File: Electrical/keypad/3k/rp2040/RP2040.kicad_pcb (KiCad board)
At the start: 4 copper layers, 64.2 x 66.2 mm, 95 parts, among them J1 Conn_01x04_Socket, J2 Conn_01x04_Socket, P1 USB-TYPE-C-016, Q1 BSS138, Q2 BSS138, SW1 KAN0644-0551B1-A, SW2 KAN0644-0551B1-A, SW3 KAN0644-0551B1-A, SW4 TS-1187A-B-A-B, SW5 TS-1187A-B-A-B, U1 ME6212C33M5G, U2 W25Q16JVSS, U3 PRTR5V0U2X, U4 RP2040, U5 SLSS49E, U6 SLSS49E, U7 SLSS49E, Y1 12MHz

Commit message: fixes stray via
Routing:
- net GND: track 66.7 -> 65.5 mm, vias 61 -> 60
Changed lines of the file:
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@@
   (via (at 92.1725 88.49) (size 0.6) (drill 0.35) (layers "F.Cu" "B.Cu") (free) (net 1))
   (via (at 97.965 108.63) (size 0.6) (drill 0.35) (layers "F.Cu" "B.Cu") (net 1))
-  (via (at 86.71 92.03) (size 0.6) (drill 0.35) (layers "F.Cu" "B.Cu") (net 1))
   (via (at 122.655 115.84) (size 0.6) (drill 0.35) (layers "F.Cu" "B.Cu") (net 1))
   (via (at 82.845662 75.97) (size 0.6) (drill 0.35) (layers "F.Cu" "B.Cu") (net 1))
@@
   (via (at 93.73 75.47) (size 0.6) (drill 0.35) (layers "F.Cu" "B.Cu") (net 1))
   (segment (start 107.645 127.98) (end 107.645 128.11) (width 0.2) (layer "B.Cu") (net 1))
-  (segment (start 86.71 92.03) (end 86.56 91.91) (width 0.2) (layer "B.Cu") (net 1))
   (segment (start 79.85 88.6) (end 79.85 88.635) (width 0.2) (layer "B.Cu") (net 1))
   (segment (start 127.505 112.63) (end 127.495 112.64) (width 0.3) (layer "B.Cu") (net 1))
@@
   (segment (start 118.81 79.74) (end 118.785 79.765) (width 0.3) (layer "B.Cu") (net 1))
   (segment (start 95.617262 123.825) (end 95.617262 123.255) (width 0.2) (layer "B.Cu") (net 1))
-  (segment (start 85.86 91.41) (end 86.06 91.41) (width 0.2) (layer "B.Cu") (net 1))
   (segment (start 122.595 115.85) (end 122.585 115.84) (width 0.2) (layer "B.Cu") (net 1))
   (segment (start 87.71 75.12) (end 87.64 75.19) (width 0.2) (layer "B.Cu") (net 1))
@@
   (segment (start 128.38 105.4) (end 129.1 105.4) (width 0.2) (layer "B.Cu") (net 1))
   (segment (start 83.61 75.97) (end 83.67 76.03) (width 0.3) (layer "B.Cu") (net 1))
-  (segment (start 86.06 91.41) (end 86.71 92.03) (width 0.2) (layer "B.Cu") (net 1))
   (segment (start 117.225 95.5) (end 118.135 95.5) (width 0.2) (layer "B.Cu") (net 1))
   (segment (start 109.13 122.945) (end 109.125 122.95) (width 0.3) (layer "B.Cu") (net 1))

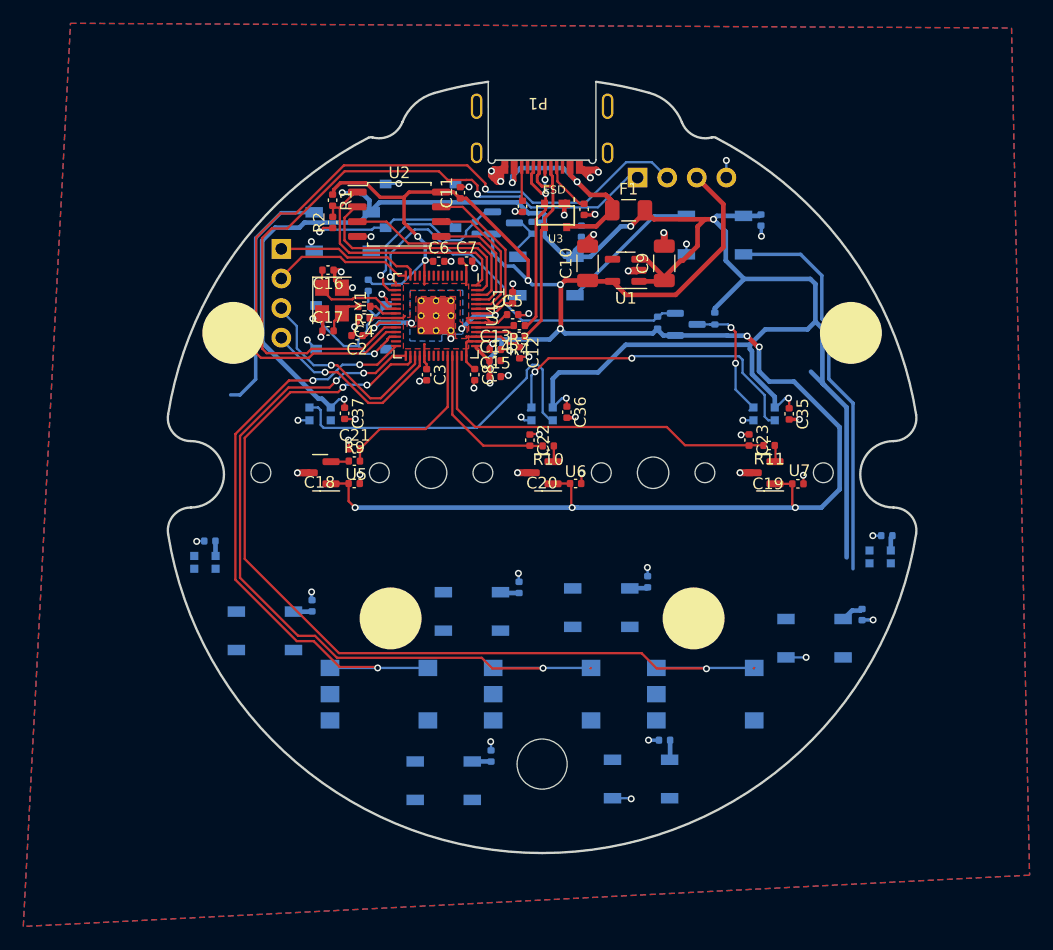
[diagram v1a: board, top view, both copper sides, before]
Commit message: puts in more led
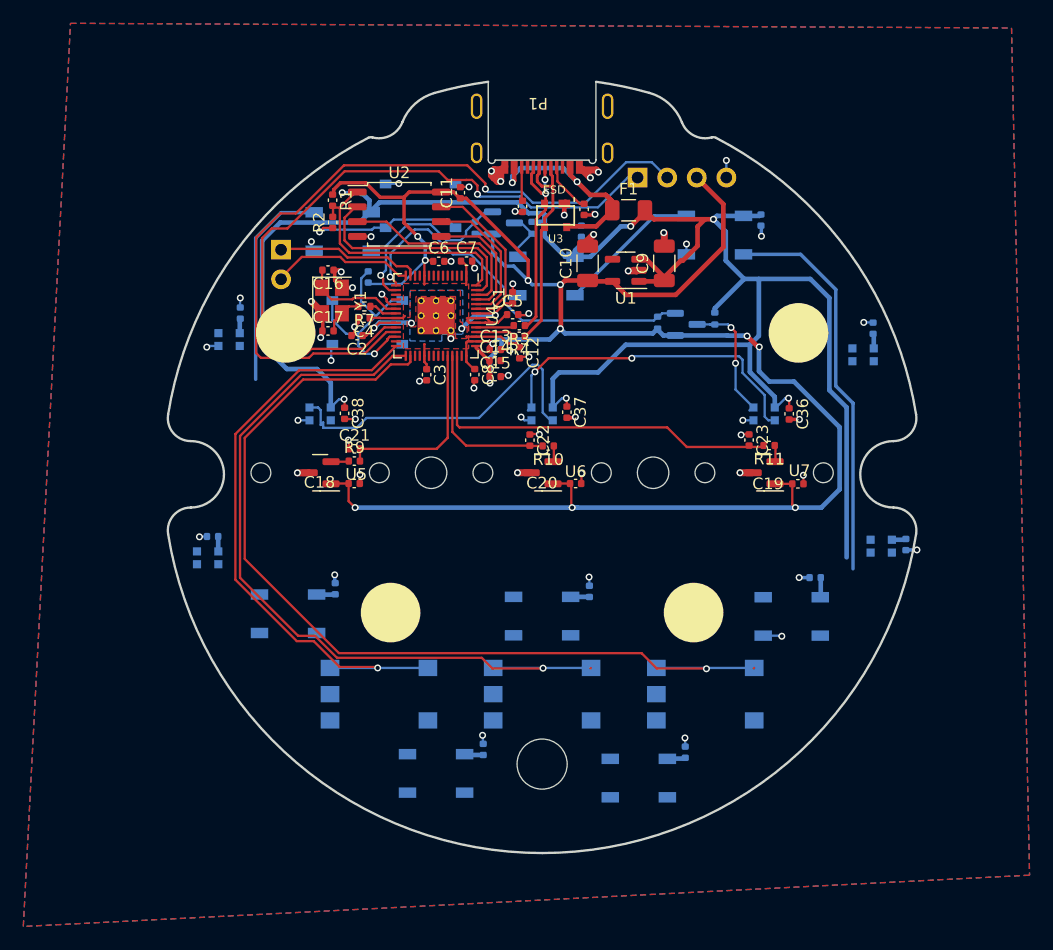
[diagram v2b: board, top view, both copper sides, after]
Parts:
- added C35: 100n, Capacitor_SMD:C_0402_1005Metric, B.Cu at (74.1, 86.3)
- added D11: WS2812-2020, footprints:LED_WS2812-2020, B.Cu at (73.1, 88.6)
- D4: value WS2812B -> WS2812-2020; footprint LED_SMD:LED_WS2812B_PLCC4_5.0x5.0mm_P3.2mm -> footprints:LED_WS2812-2020
- J1: value Conn_01x04_Socket -> Conn_01x02_Socket; footprint Connector_PinSocket_2.54mm:PinSocket_1x04_P2.54mm_Vertical -> Connector_PinSocket_2.54mm:PinSocket_1x02_P2.54mm_Vertical
- moved C28 19.0 mm to (123.4, 109.0)
- moved D5 19.0 mm to (121.4, 112.3)
- moved C26 17.8 mm to (128.4, 87.6), turned to 90 degrees
- moved D3 17.4 mm to (127.5, 89.9)
- moved C30 16.5 mm to (104.1, 110.2)
- moved D7 16.5 mm to (100.0, 112.3)
- moved C32 15.0 mm to (112.3, 124.0)
- moved D6 15.0 mm to (108.3, 126.2)
- moved C31 14.2 mm to (94.9, 123.7)
- moved D8 14.2 mm to (90.9, 125.8)
- moved D4 9.76 mm to (129.1, 106.3), turned to 0 degrees
- moved C27 7.09 mm to (131.2, 106.2)
- moved REF** 4.50 mm to (122.0, 88.0)
- moved REF** 4.45 mm to (78.0, 88.0)
- moved C29 2.47 mm to (82.2, 110.0)
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- renumbered C35 to C36, C36 to C37, C37 to C38, D11 to D12, D12 to D13, D13 to D14, D14 to D15
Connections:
- D12 pad 4: Net-(D10-DO) -> Net-(D11-DO)
- U4 pad 31: SDA_0 -> /GPIO20
- U4 pad 32: SCL_0 -> /GPIO21
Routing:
- net Net-(D10-DO): track 20.6 -> 0.00 mm
- net SDA_0: track 17.9 -> 0.00 mm, vias 1 -> 0
- net Net-(D11-DO): track 0.00 -> 17.9 mm
- net SCL_0: track 16.6 -> 0.00 mm, vias 1 -> 0
- net Net-(U4-RUN): track 16.8 -> 19.2 mm
- net ADC_IN1: track 14.4 -> 16.0 mm
- net ADC_IN2: track 13.9 -> 14.8 mm
- net ADC_IN3: track 32.3 -> 33.1 mm
- net GND: track 65.5 -> 65.9 mm, vias 60 -> 61
- net BUTT2: vias 3 -> 1
- net BUTT0: vias 3 -> 1
- net BUTT1: vias 3 -> 1

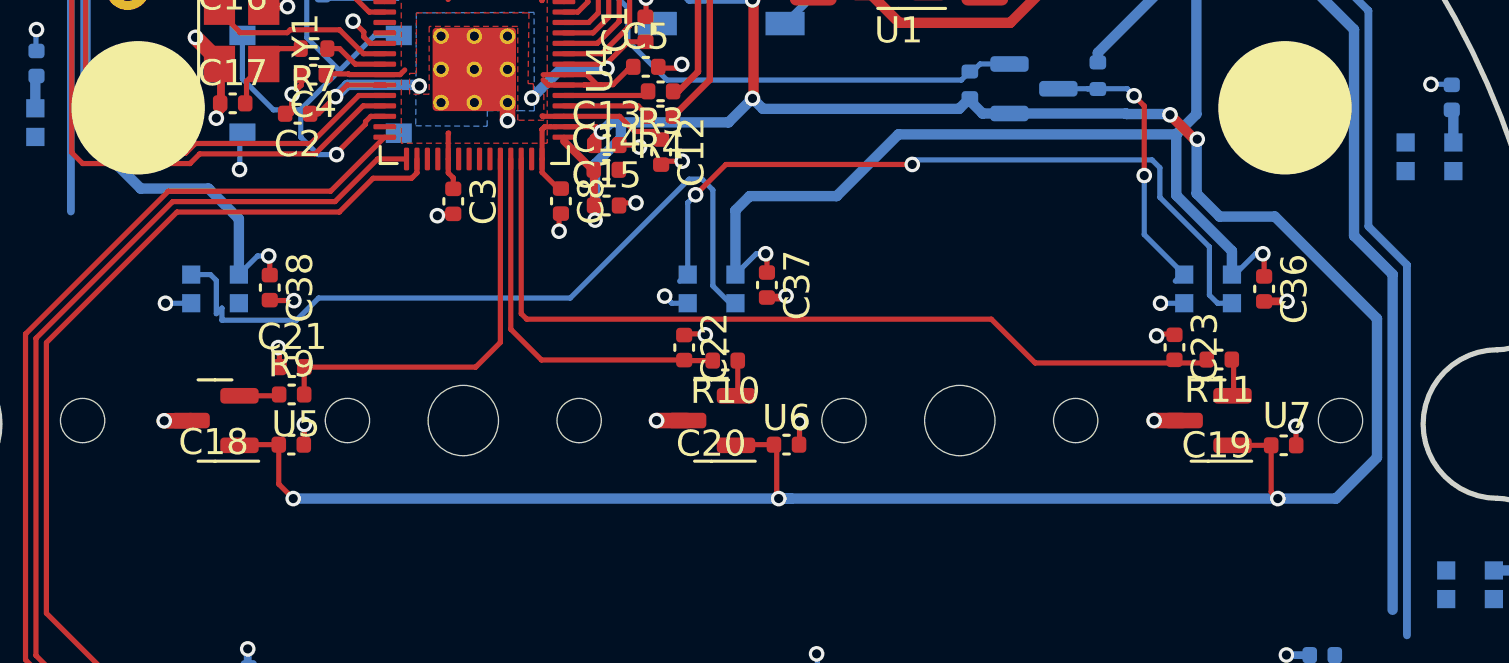
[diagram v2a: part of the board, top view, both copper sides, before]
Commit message: reorient HE sensors
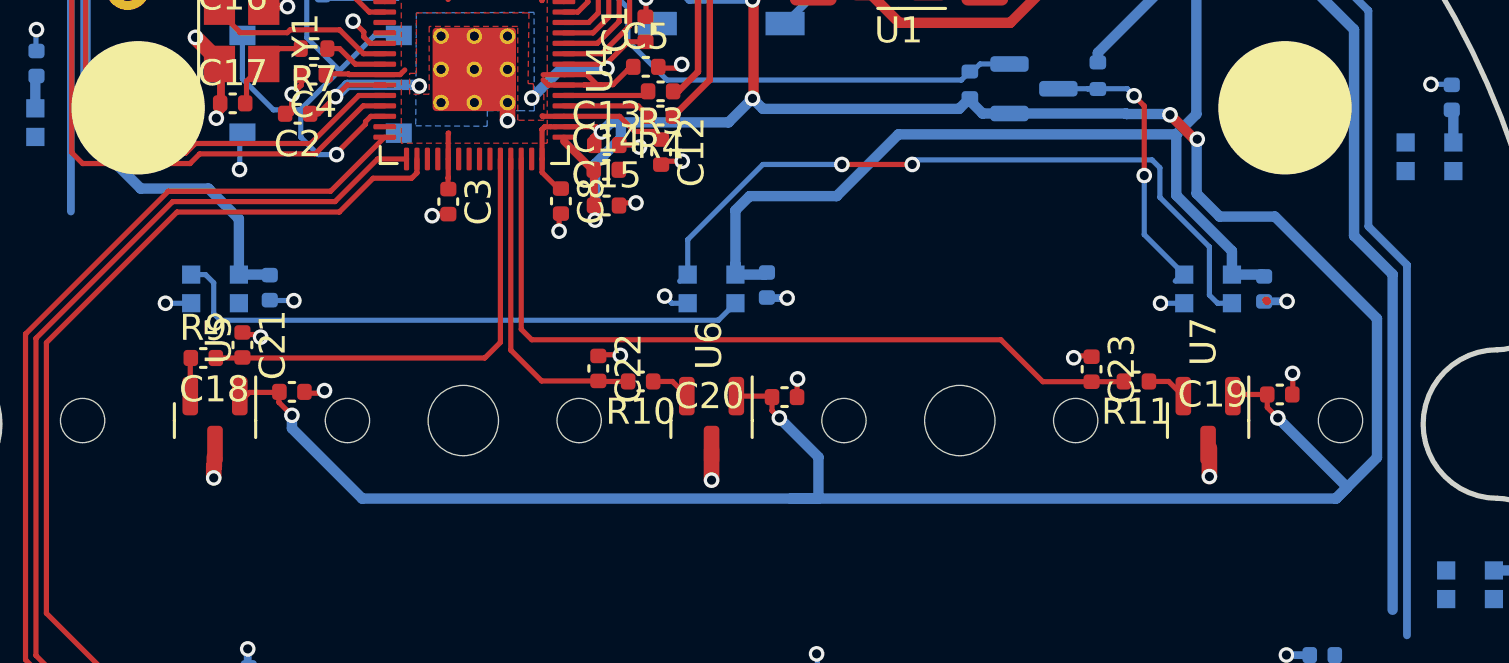
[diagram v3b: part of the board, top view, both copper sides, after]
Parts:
- C36, C37, C38: moved to B.Cu
- moved R9 3.67 mm to (80.5, 97.6)
- moved C22 3.39 mm to (95.7, 98.0)
- moved R10 3.34 mm to (97.3, 98.5)
- moved C23 3.29 mm to (114.6, 98.0)
- moved R11 3.29 mm to (116.3, 98.5)
- moved C21 2.08 mm to (82.0, 97.1), turned to -90 degrees
- moved C18 2.03 mm to (83.9, 98.9)
- moved C19 1.96 mm to (121.8, 99.0)
- moved C20 1.83 mm to (102.8, 99.1)
- moved C3 0.19 mm to (89.9, 91.6)
- turned U5 to -90 degrees
- turned U6 to -90 degrees
- turned U7 to -90 degrees
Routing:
- net Net-(D14-DO): track 29.2 -> 22.6 mm
- net +3V3: track 195.0 -> 201.4 mm
- net +5V: track 179.1 -> 175.9 mm, vias 5 -> 2
- net ADC_IN2: track 14.8 -> 12.3 mm
- net ADC_IN3: track 33.1 -> 30.7 mm
- net ADC_IN1: track 16.0 -> 18.2 mm
- net Net-(D13-DO): track 28.6 -> 27.8 mm
- net GND: track 65.9 -> 65.1 mm

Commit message: misc changes
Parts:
- moved C34 0.71 mm to (84.8, 76.0)
- moved J1 0.52 mm to (78.0, 81.2)
- moved D12 0.46 mm to (83.3, 79.3)
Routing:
- net Net-(R2-Pad1): track 13.7 -> 12.3 mm
- net GND: track 65.1 -> 66.2 mm
- net +5V: track 175.9 -> 175.3 mm

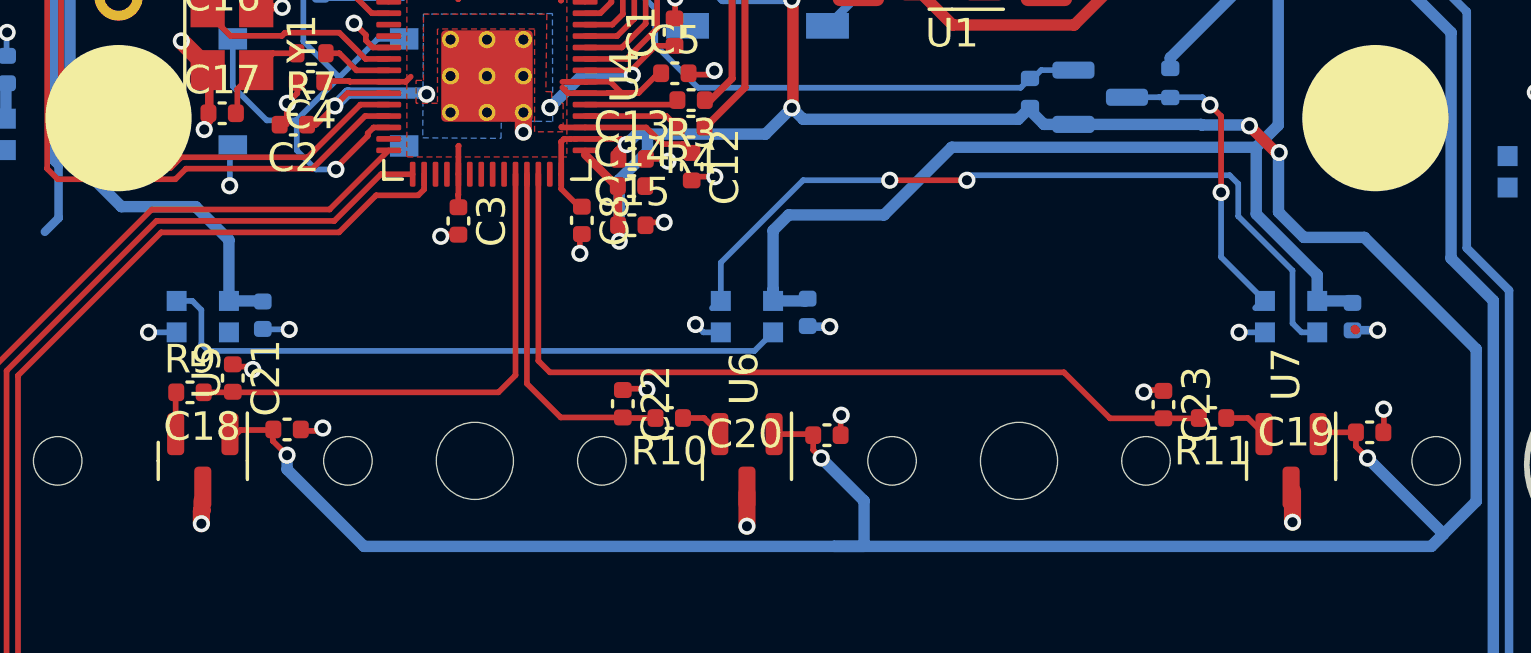
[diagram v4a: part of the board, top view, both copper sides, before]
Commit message: changes trace width of analog signals to be 0.3
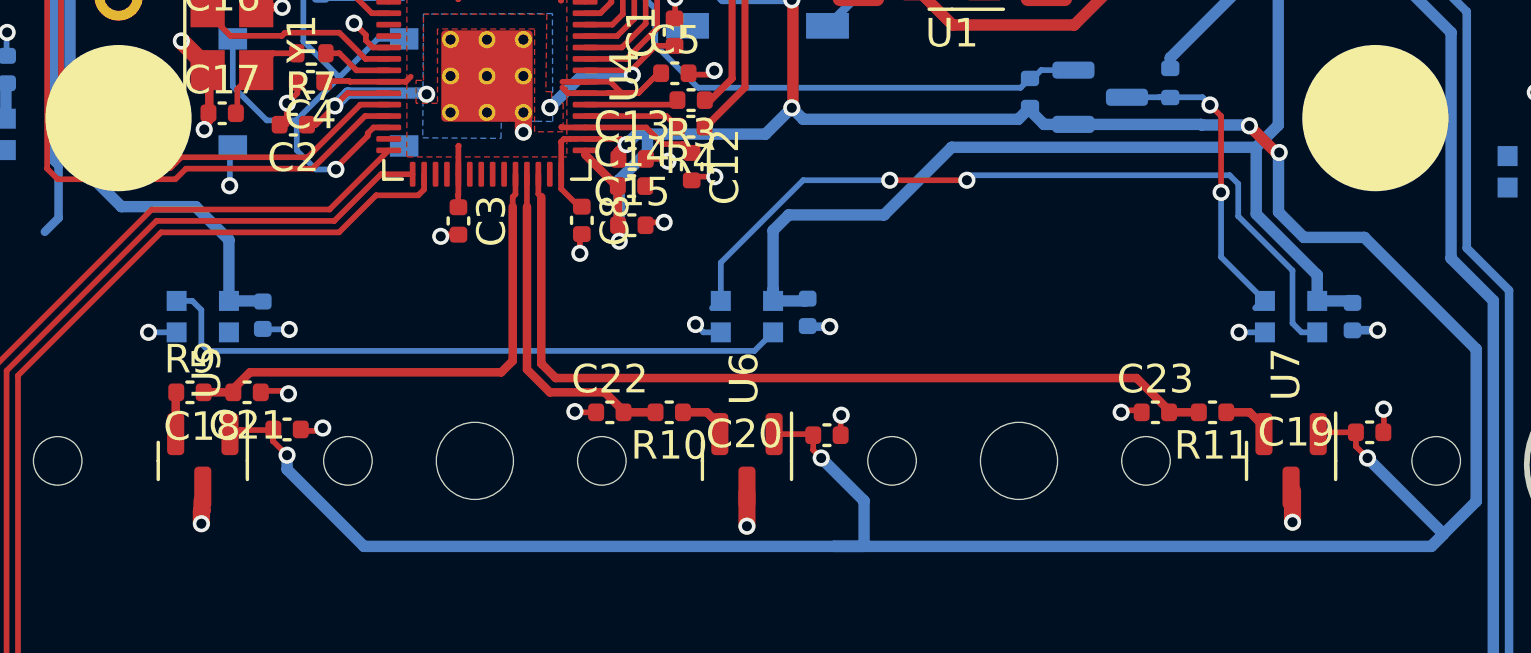
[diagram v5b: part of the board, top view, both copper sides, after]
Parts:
- moved C21 0.71 mm to (82.5, 97.6), turned to 180 degrees
- moved C22 0.54 mm to (95.2, 98.3), turned to 0 degrees
- moved C23 0.39 mm to (114.3, 98.3), turned to 0 degrees
- moved R10 0.20 mm to (97.3, 98.3)
- moved R11 0.20 mm to (116.3, 98.3)

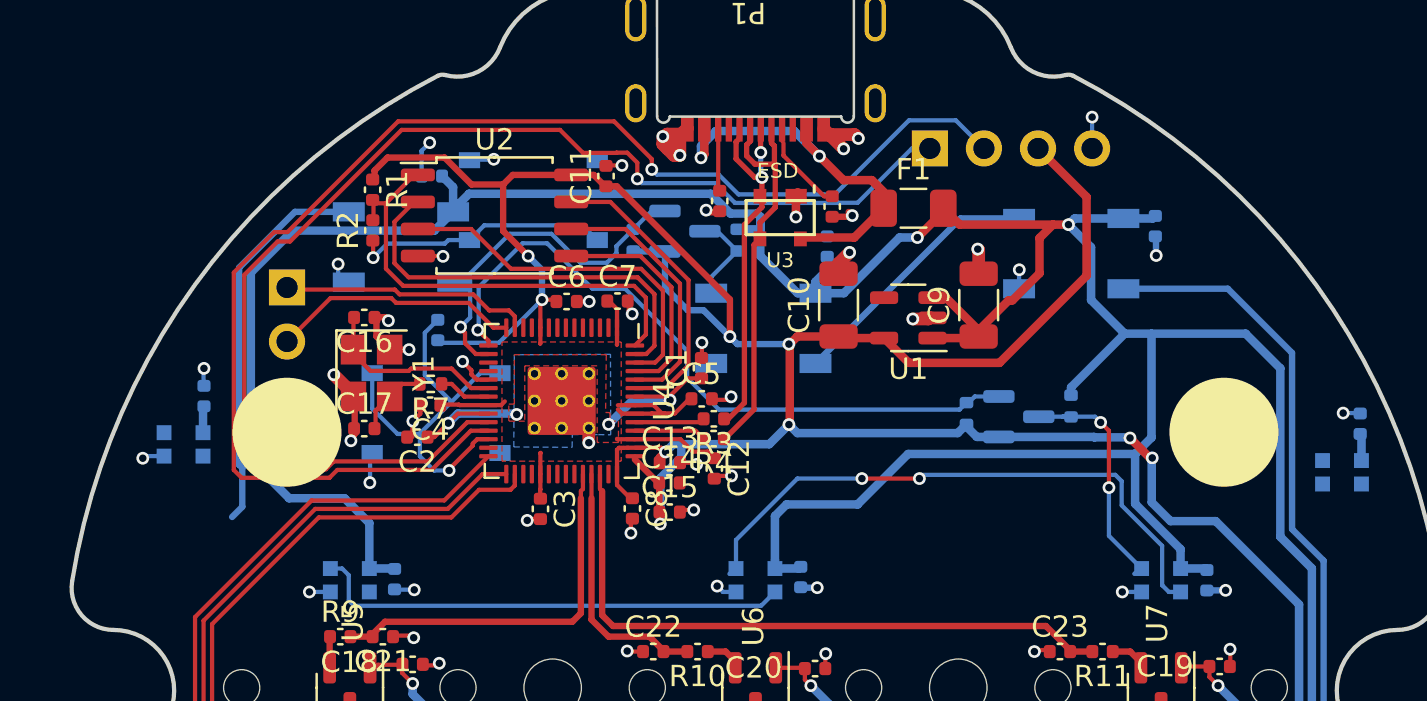
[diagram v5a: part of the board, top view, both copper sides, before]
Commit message: reorganize some components for better fit
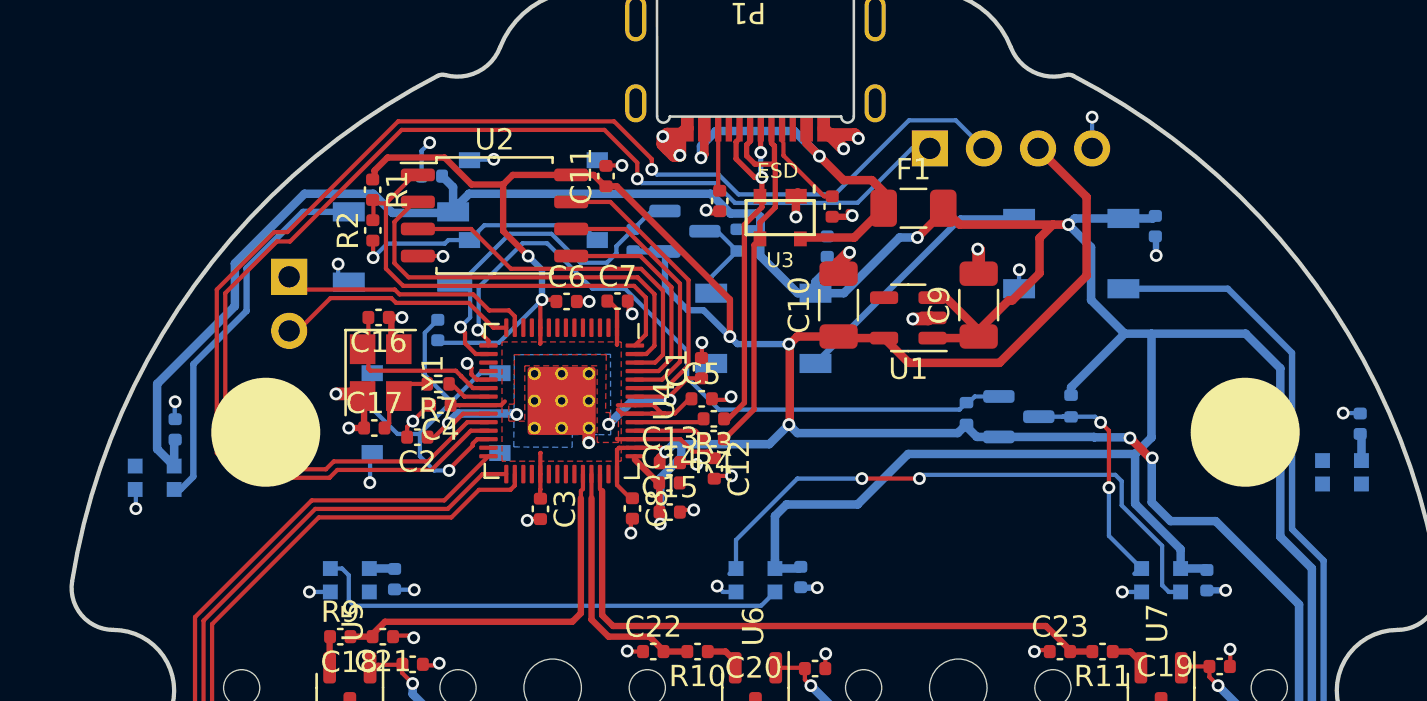
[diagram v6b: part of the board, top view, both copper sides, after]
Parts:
- REF**: moved to B.Cu
- moved D11 2.07 mm to (71.8, 90.1)
- moved C35 2.07 mm to (72.7, 87.9)
- moved REF** 1.10 mm to (76.9, 88.0), turned to 180 degrees
- moved REF** 1.00 mm to (123.0, 88.0)
- moved C16 0.67 mm to (82.3, 82.6)
- moved J1 0.51 mm to (78.1, 80.7)
- moved C4 0.48 mm to (85.2, 86.7)
- moved C17 0.47 mm to (82.1, 87.8)
- moved Y1 0.43 mm to (82.4, 85.2)
- moved R7 0.35 mm to (85.1, 85.7)
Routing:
- net +5V: track 175.3 -> 170.3 mm
- net GND: track 66.1 -> 64.5 mm, vias 61 -> 60
- net Net-(C17-Pad2): track 4.37 -> 3.35 mm
- net SWCLK: track 59.3 -> 60.2 mm
- net SWDIO: track 64.3 -> 64.9 mm
- net +3V3: track 201.4 -> 200.8 mm
